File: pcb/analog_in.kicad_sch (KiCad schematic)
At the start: 21 parts, among them J7 Guitar Input, J8 Guitar Output, U5 TL072

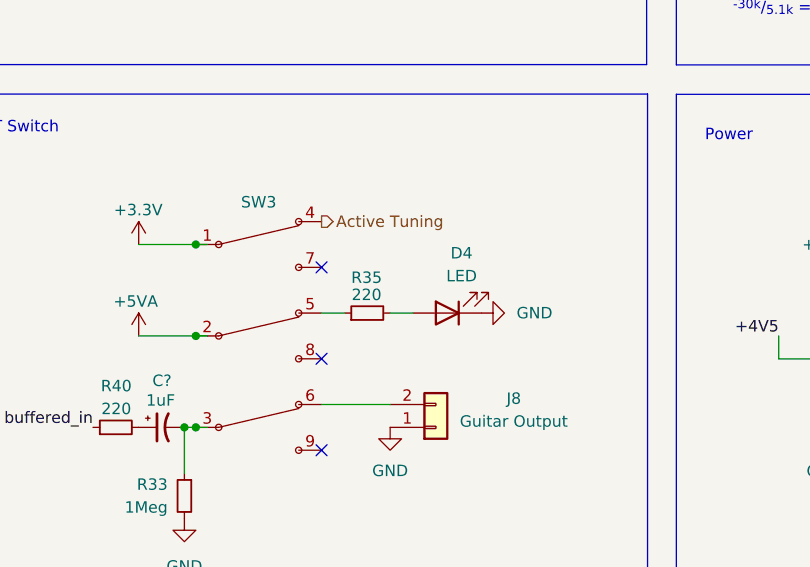
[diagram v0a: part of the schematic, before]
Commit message: trying to isolate analog from noise sources
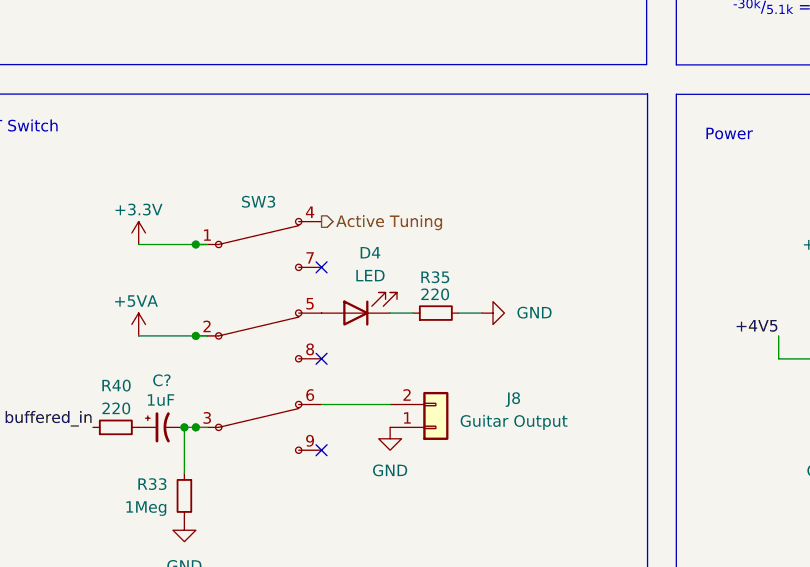
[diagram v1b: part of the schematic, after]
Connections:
- net GND: now also R35.2; no longer D4.1 (K)
- net at SW3.5: now also D4.2 (A); no longer R35.1
- new net: D4.1 (K), R35.1
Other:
- moved on the sheet: D4, R35
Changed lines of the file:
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@@
   (no_connect (at 111.76 124.46))
   (no_connect (at 111.76 134.62))
-  (wire (pts (xy 119.38 119.38) (xy 121.92 119.38))
-    (stroke (width 0) (type default))
-  )
   (wire (pts (xy 213.36 58.42) (xy 213.36 63.5))
     (stroke (width 0) (type default))
@@
     (stroke (width 0) (type default))
   )
-  (wire (pts (xy 111.76 119.38) (xy 114.3 119.38))
-    (stroke (width 0) (type default))
-  )
   (wire (pts (xy 175.26 60.96) (xy 177.8 60.96))
     (stroke (width 0) (type default))
@@
     (stroke (width 0) (type default))
   )
+  (wire (pts (xy 127 119.38) (xy 129.54 119.38))
+    (stroke (width 0) (type default))
+  )
   (wire (pts (xy 91.44 111.76) (xy 97.79 111.76))
     (stroke (width 0) (type default))
@@
   )
   (wire (pts (xy 86.36 71.12) (xy 86.36 63.5))
+    (stroke (width 0) (type default))
+  )
+  (wire (pts (xy 121.92 119.38) (xy 119.38 119.38))
     (stroke (width 0) (type default))
   )
@@
     )
   )
-  (symbol (lib_id "Device:LED") (at 125.73 119.38 180) (unit 1)
-    (in_bom yes) (on_board yes) (dnp no) (fields_autoplaced)
-    (property "Reference" "D4" (at 127.3175 112.7252 0)
-      (effects (font (size 1.27 1.27)))
-    )
-    (property "Value" "LED" (at 127.3175 115.2652 0)
-      (effects (font (size 1.27 1.27)))
-    )
-    (property "Footprint" "Connector_PinHeader_2.54mm:PinHeader_1x02_P2.54mm_Vertical" (at 125.73 119.38 0)
-      (effects (font (size 1.27 1.27)) hide)
-    )
-    (property "Datasheet" "~" (at 125.73 119.38 0)
-      (effects (font (size 1.27 1.27)) hide)
-    )
-    (property "DNP" "" (at 125.73 119.38 0)
-      (effects (font (size 1.27 1.27)) hide)
-    )
-    (property "LCSC" "" (at 125.73 119.38 0)
+  (symbol (lib_id "Device:LED") (at 115.57 119.38 180) (unit 1)
+    (in_bom yes) (on_board yes) (dnp no) (fields_autoplaced)
+    (property "Reference" "D4" (at 117.1575 112.7252 0)
+      (effects (font (size 1.27 1.27)))
+    )
+    (property "Value" "LED" (at 117.1575 115.2652 0)
+      (effects (font (size 1.27 1.27)))
+    )
+    (property "Footprint" "Connector_PinHeader_2.54mm:PinHeader_1x02_P2.54mm_Vertical" (at 115.57 119.38 0)
+      (effects (font (size 1.27 1.27)) hide)
+    )
+    (property "Datasheet" "~" (at 115.57 119.38 0)
+      (effects (font (size 1.27 1.27)) hide)
+    )
+    (property "DNP" "" (at 115.57 119.38 0)
+      (effects (font (size 1.27 1.27)) hide)
+    )
+    (property "LCSC" "" (at 115.57 119.38 0)
       (effects (font (size 1.27 1.27)) hide)
     )
@@
     )
   )
-  (symbol (lib_id "Device:R_Small") (at 116.84 119.38 90) (unit 1)
+  (symbol (lib_id "Device:R_Small") (at 124.46 119.38 90) (unit 1)
     (in_bom yes) (on_board yes) (dnp no)
-    (property "Reference" "R35" (at 116.7638 115.443 90)
-      (effects (font (size 1.27 1.27)))
-    )
-    (property "Value" "220" (at 116.7638 117.348 90)
-      (effects (font (size 1.27 1.27)))
-    )
-    (property "Footprint" "Resistor_SMD:R_0603_1608Metric" (at 116.84 119.38 0)
-      (effects (font (size 1.27 1.27)) hide)
-    )
-    (property "Datasheet" "~" (at 116.84 119.38 0)
-      (effects (font (size 1.27 1.27)) hide)
-    )
-    (property "MPN" "RC0603FR-07220RL" (at 116.84 119.38 0)
-      (effects (font (size 1.27 1.27)) hide)
-    )
-    (property "Manufacturer" "Yageo" (at 116.84 119.38 0)
-      (effects (font (size 1.27 1.27)) hide)
-    )
-    (property "DNP" "" (at 116.84 119.38 0)
-      (effects (font (size 1.27 1.27)) hide)
-    )
-    (property "LCSC" "C107696" (at 116.84 119.38 0)
-      (effects (font (size 1.27 1.27)) hide)
-    )
+    (property "Reference" "R35" (at 124.3838 115.443 90)
+      (effects (font (size 1.27 1.27)))
+    )
+    (property "Value" "220" (at 124.3838 117.348 90)
+      (effects (font (size 1.27 1.27)))
+    )
+    (property "Footprint" "Resistor_SMD:R_0603_1608Metric" (at 124.46 119.38 0)
+      (effects (font (size 1.27 1.27)) hide)
+    )
+    (property "Datasheet" "~" (at 124.46 119.38 0)
+      (effects (font (size 1.27 1.27)) hide)
+    )
+    (property "MPN" "RC0603FR-07220RL" (at 124.46 119.38 0)
+      (effects (font (size 1.27 1.27)) hide)
+    )
+    (property "Manufacturer" "Yageo" (at 124.46 119.38 0)
+      (effects (font (size 1.27 1.27)) hide)
+    )
+    (property "DNP" "" (at 124.46 119.38 0)
+      (effects (font (size 1.27 1.27)) hide)
+    )
+    (property "LCSC" "C107696" (at 124.46 119.38 0)
+      (effects (font (size 1.27 1.27)) hide)
+    )

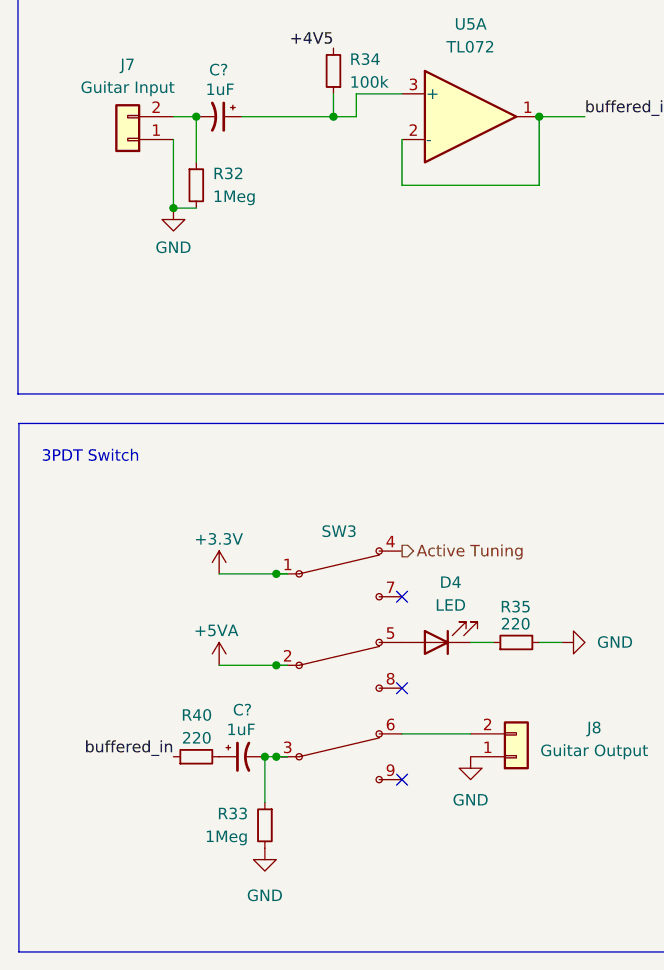
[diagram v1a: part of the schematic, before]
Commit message: Lowered resistor values and added protection diode
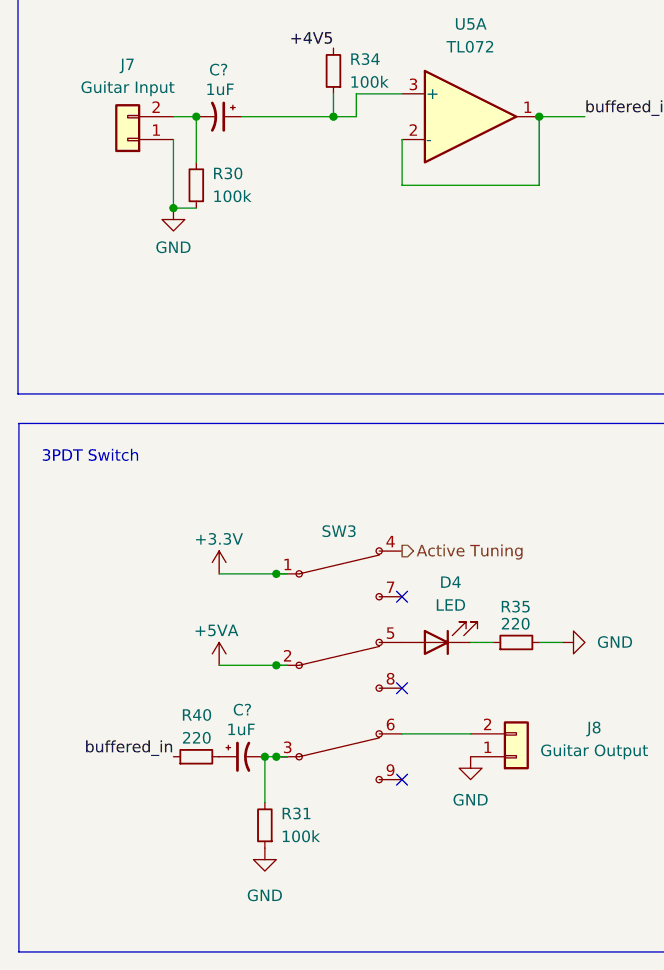
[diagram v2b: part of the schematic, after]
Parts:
- removed R32, R33: 1Meg, Resistor_SMD:R_0603_1608Metric, symbol Device:R_Small
- added R30, R31: 100k, Resistor_SMD:R_0603_1608Metric, symbol Device:R_Small
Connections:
- net GND: now also R30.1, R31.1
- net at C?.2, SW3.3: now also R31.2
- net at C?.2, J7.2 (Pin_2): now also R30.2
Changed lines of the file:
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@@
-    )
-  )
-  (symbol (lib_id "Device:R_Small") (at 88.9 68.58 0) (unit 1)
-    (in_bom yes) (on_board yes) (dnp no) (fields_autoplaced)
-    (property "Reference" "R32" (at 90.7542 67.31 0)
-      (effects (font (size 1.27 1.27)) (justify left))
-    )
-    (property "Value" "1Meg" (at 90.7542 69.85 0)
-      (effects (font (size 1.27 1.27)) (justify left))
-    )
-    (property "Footprint" "Resistor_SMD:R_0603_1608Metric" (at 88.9 68.58 0)
-      (effects (font (size 1.27 1.27)) hide)
-    )
-    (property "Datasheet" "~" (at 88.9 68.58 0)
-      (effects (font (size 1.27 1.27)) hide)
-    )
-    (property "MPN" "RC0603FR-071ML" (at 88.9 68.58 0)
-      (effects (font (size 1.27 1.27)) hide)
-    )
-    (property "Manufacturer" "Yageo" (at 88.9 68.58 0)
-      (effects (font (size 1.27 1.27)) hide)
-    )
-    (property "DNP" "" (at 88.9 68.58 0)
-      (effects (font (size 1.27 1.27)) hide)
-    )
-    (property "LCSC" "C105578" (at 88.9 68.58 0)
-      (effects (font (size 1.27 1.27)) hide)
-    )
-    (pin "1")
-    (pin "2")
-    (instances
-      (project "tuner_pedal"
-        (path "/be09f3cc-c79c-49de-93a4-4a01bf6bfbcf/3d167967-9605-4205-bbbf-27792cf0ebc1"
-          (reference "R32") (unit 1)
-        )
-      )
     )
   )
@@
         (path "/be09f3cc-c79c-49de-93a4-4a01bf6bfbcf/3d167967-9605-4205-bbbf-27792cf0ebc1"
           (reference "#PWR070") (unit 1)
-        )
-      )
-    )
-  )
-  (symbol (lib_id "Device:R_Small") (at 96.52 139.7 0) (mirror y) (unit 1)
-    (in_bom yes) (on_board yes) (dnp no) (fields_autoplaced)
-    (property "Reference" "R33" (at 94.6658 138.43 0)
-      (effects (font (size 1.27 1.27)) (justify left))
-    )
-    (property "Value" "1Meg" (at 94.6658 140.97 0)
-      (effects (font (size 1.27 1.27)) (justify left))
-    )
-    (property "Footprint" "Resistor_SMD:R_0603_1608Metric" (at 96.52 139.7 0)
-      (effects (font (size 1.27 1.27)) hide)
-    )
-    (property "Datasheet" "~" (at 96.52 139.7 0)
-      (effects (font (size 1.27 1.27)) hide)
-    )
-    (property "MPN" "RC0603FR-071ML" (at 96.52 139.7 0)
-      (effects (font (size 1.27 1.27)) hide)
-    )
-    (property "Manufacturer" "Yageo" (at 96.52 139.7 0)
-      (effects (font (size 1.27 1.27)) hide)
-    )
-    (property "DNP" "" (at 96.52 139.7 0)
-      (effects (font (size 1.27 1.27)) hide)
-    )
-    (property "LCSC" "C105578" (at 96.52 139.7 0)
-      (effects (font (size 1.27 1.27)) hide)
-    )
-    (pin "1")
-    (pin "2")
-    (instances
-      (project "tuner_pedal"
-        (path "/be09f3cc-c79c-49de-93a4-4a01bf6bfbcf/3d167967-9605-4205-bbbf-27792cf0ebc1"
-          (reference "R33") (unit 1)
         )
       )
@@
     )
   )
+  (symbol (lib_id "Device:R_Small") (at 88.9 68.58 180) (unit 1)
+    (in_bom yes) (on_board yes) (dnp no) (fields_autoplaced)
+    (property "Reference" "R30" (at 90.7034 67.31 0)
+      (effects (font (size 1.27 1.27)) (justify right))
+    )
+    (property "Value" "100k" (at 90.7034 69.85 0)
+      (effects (font (size 1.27 1.27)) (justify right))
+    )
+    (property "Footprint" "Resistor_SMD:R_0603_1608Metric" (at 88.9 68.58 0)
+      (effects (font (size 1.27 1.27)) hide)
+    )
+    (property "Datasheet" "~" (at 88.9 68.58 0)
+      (effects (font (size 1.27 1.27)) hide)
+    )
+    (property "MPN" "RC0603FR-07100KL" (at 88.9 68.58 0)
+      (effects (font (size 1.27 1.27)) hide)
+    )
+    (property "Manufacturer" "Yageo" (at 88.9 68.58 0)
+      (effects (font (size 1.27 1.27)) hide)
+    )
+    (property "DNP" "" (at 88.9 68.58 0)
+      (effects (font (size 1.27 1.27)) hide)
+    )
+    (property "LCSC" "C14675" (at 88.9 68.58 0)
+      (effects (font (size 1.27 1.27)) hide)
+    )
+    (pin "1")
+    (pin "2")
+    (instances
+      (project "tuner_pedal"
+        (path "/be09f3cc-c79c-49de-93a4-4a01bf6bfbcf/3d167967-9605-4205-bbbf-27792cf0ebc1"
+          (reference "R30") (unit 1)
+        )
+      )
+    )
+  )
   (symbol (lib_id "Device:R_Small") (at 167.64 60.96 90) (unit 1)
     (in_bom yes) (on_board yes) (dnp no) (fields_autoplaced)
@@
         )
       )
+    )
+  )
+  (symbol (lib_id "Device:R_Small") (at 96.52 139.7 180) (unit 1)
+    (in_bom yes) (on_board yes) (dnp no) (fields_autoplaced)
+    (property "Reference" "R31" (at 98.3234 138.43 0)
+      (effects (font (size 1.27 1.27)) (justify right))
+    )
+    (property "Value" "100k" (at 98.3234 140.97 0)
+      (effects (font (size 1.27 1.27)) (justify right))
+    )
+    (property "Footprint" "Resistor_SMD:R_0603_1608Metric" (at 96.52 139.7 0)
+      (effects (font (size 1.27 1.27)) hide)
+    )
+    (property "Datasheet" "~" (at 96.52 139.7 0)
+      (effects (font (size 1.27 1.27)) hide)
+    )
+    (property "MPN" "RC0603FR-07100KL" (at 96.52 139.7 0)
+      (effects (font (size 1.27 1.27)) hide)
+    )
+    (property "Manufacturer" "Yageo" (at 96.52 139.7 0)
+      (effects (font (size 1.27 1.27)) hide)
+    )
+    (property "DNP" "" (at 96.52 139.7 0)
+      (effects (font (size 1.27 1.27)) hide)
+    )
+    (property "LCSC" "C14675" (at 96.52 139.7 0)
+      (effects (font (size 1.27 1.27)) hide)
+    )
+    (pin "1")
+    (pin "2")
+    (instances
+      (project "tuner_pedal"
+        (path "/be09f3cc-c79c-49de-93a4-4a01bf6bfbcf/3d167967-9605-4205-bbbf-27792cf0ebc1"
+          (reference "R31") (unit 1)
+        )
+      )
